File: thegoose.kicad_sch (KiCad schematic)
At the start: 45 parts, among them U1 DRV8848, U2 DRV8848, U3 DRV8848, U4 AP64500SP-13

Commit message: Connect everything except GPIO
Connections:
- net ESP_D12: no longer U1.9 (BIN1)
- net ESP_D13: no longer U1.10 (BIN2)
- net ESP_D14: no longer U1.15 (AIN2)
- net ESP_D15: no longer S6.1 (Pin_1)
- net ESP_D16: no longer S2.1 (Pin_1)
- net ESP_D17: no longer S3.1 (Pin_1)
- net ESP_D18: no longer S5.1 (Pin_1)
- net ESP_D19: no longer U3.16 (AIN1)
- net ESP_D21: no longer U3.15 (AIN2)
- net ESP_D22: no longer U3.9 (BIN1)
- net ESP_D23: no longer U3.10 (BIN2)
- net ESP_D25: no longer U2.9 (BIN1)
- net ESP_D26: no longer U2.10 (BIN2)
- net ESP_D27: no longer U1.16 (AIN1)
- net ESP_D32: no longer U2.16 (AIN1)
- net ESP_D33: no longer U2.15 (AIN2)
- net ESP_D4: no longer S1.1 (Pin_1)
- net ESP_D5: no longer S4.1 (Pin_1)
- net at U3.5 (BOUT2): now also M6.1 (OUT1); no longer M6.2 (OUT2)
- net at U3.7 (BOUT1): now also M6.2 (OUT2); no longer M6.1 (OUT1)
- net at M2.1 (OUT1): now also U1.5 (BOUT2); no longer U1.7 (BOUT1)
- net at M2.2 (OUT2): now also U1.7 (BOUT1); no longer U1.5 (BOUT2)
- net at M4.1 (OUT1): now also U2.5 (BOUT2); no longer U2.7 (BOUT1)
- net at M4.2 (OUT2): now also U2.7 (BOUT1); no longer U2.5 (BOUT2)

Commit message: Disconnect GPIO on schematic
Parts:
- removed C12, C5, C8: 100uF, Capacitor_SMD:C_1206_3216Metric_Pad1.33x1.80mm_HandSolder, symbol Device:C_Polarized

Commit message: First iteration of PCB
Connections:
- net ESP_D12: now also S2.1 (Pin_1)
- net ESP_D13: now also S1.1 (Pin_1)
- net ESP_D14: now also U3.15 (AIN2)
- net ESP_D15: now also U1.9 (BIN1)
- net ESP_D16: now also U1.15 (AIN2)
- net ESP_D17: now also U1.16 (AIN1)
- net ESP_D18: now also U2.10 (BIN2)
- net ESP_D19: now also U2.15 (AIN2)
- net ESP_D21: now also U2.16 (AIN1)
- net ESP_D22: now also U3.9 (BIN1)
- net ESP_D23: now also U3.10 (BIN2)
- net ESP_D25: now also S4.1 (Pin_1)
- net ESP_D26: now also S3.1 (Pin_1)
- net ESP_D27: now also U3.16 (AIN1)
- net ESP_D32: now also S6.1 (Pin_1)
- net ESP_D33: now also S5.1 (Pin_1)
- net ESP_D4: now also U1.10 (BIN2)
- net ESP_D5: now also U2.9 (BIN1)
- net at M3.1 (OUT1): now also U2.5 (BOUT2); no longer U2.2 (AOUT1)
- net at M3.2 (OUT2): now also U2.7 (BOUT1); no longer U2.4 (AOUT2)
- net at U3.2 (AOUT1): now also M6.1 (OUT1); no longer M5.1 (OUT1)
- net at U3.4 (AOUT2): now also M6.2 (OUT2); no longer M5.2 (OUT2)
- net at U3.5 (BOUT2): now also M5.1 (OUT1); no longer M6.1 (OUT1)
- net at U3.7 (BOUT1): now also M5.2 (OUT2); no longer M6.2 (OUT2)
- net at M2.1 (OUT1): now also U1.2 (AOUT1); no longer U1.5 (BOUT2)
- net at M2.2 (OUT2): now also U1.4 (AOUT2); no longer U1.7 (BOUT1)
- net at M4.1 (OUT1): now also U2.2 (AOUT1); no longer U2.5 (BOUT2)
- net at M4.2 (OUT2): now also U2.4 (AOUT2); no longer U2.7 (BOUT1)
- net at M1.1 (OUT1): now also U1.5 (BOUT2); no longer U1.2 (AOUT1)
- net at M1.2 (OUT2): now also U1.7 (BOUT1); no longer U1.4 (AOUT2)
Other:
- moved on the sheet: M1, M2, M3, M4, M5, M6

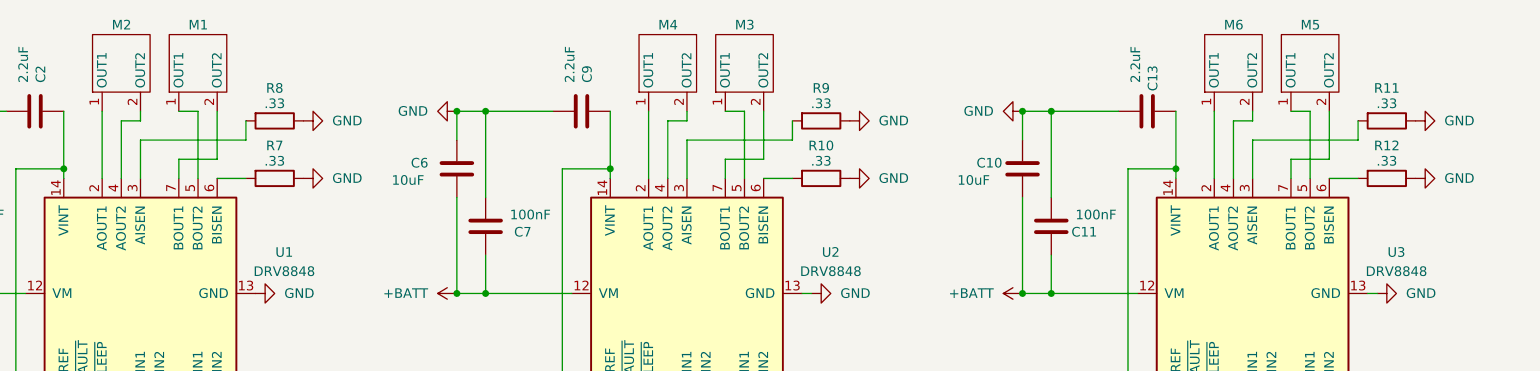
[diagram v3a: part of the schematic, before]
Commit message: Remove current shunt resistors
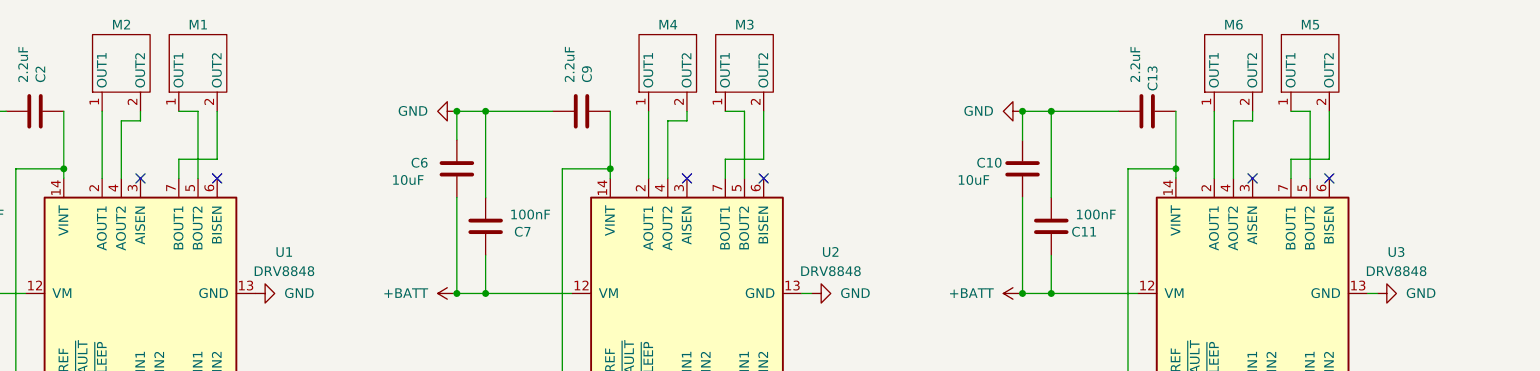
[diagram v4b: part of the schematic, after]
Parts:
- removed R10, R11, R12, R7, R8, R9: .33, Resistor_SMD:R_0805_2012Metric_Pad1.20x1.40mm_HandSolder, symbol Device:R
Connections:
- no-connect marks 10 -> 16

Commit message: Newify layout
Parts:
- BT1: value XT30_SOLDER_CABLE -> XT60; footprint hexy:XT30_SolderPads_1x02_P5.00mm -> hexy:AMASS_XT60PW-M_1x02_P7.20mm_Horizontal
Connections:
- net ESP_D15: now also U1.16 (AIN1); no longer U1.9 (BIN1)
- net ESP_D16: now also U1.9 (BIN1); no longer U1.15 (AIN2)
- net ESP_D17: now also U1.10 (BIN2); no longer U1.16 (AIN1)
- net ESP_D18: now also U2.15 (AIN2); no longer U2.10 (BIN2)
- net ESP_D19: now also U2.9 (BIN1); no longer U2.15 (AIN2)
- net ESP_D21: now also U2.10 (BIN2); no longer U2.16 (AIN1)
- net ESP_D22: now also U3.10 (BIN2); no longer U3.9 (BIN1)
- net ESP_D23: now also U3.9 (BIN1); no longer U3.10 (BIN2)
- net ESP_D4: now also U1.15 (AIN2); no longer U1.10 (BIN2)
- net ESP_D5: now also U2.16 (AIN1); no longer U2.9 (BIN1)
- net at M3.1 (OUT1): now also U2.2 (AOUT1); no longer U2.5 (BOUT2)
- net at M3.2 (OUT2): now also U2.4 (AOUT2); no longer U2.7 (BOUT1)
- net at U3.2 (AOUT1): now also M5.1 (OUT1); no longer M6.1 (OUT1)
- net at U3.4 (AOUT2): now also M5.2 (OUT2); no longer M6.2 (OUT2)
- net at U3.5 (BOUT2): now also M6.1 (OUT1); no longer M5.1 (OUT1)
- net at U3.7 (BOUT1): now also M6.2 (OUT2); no longer M5.2 (OUT2)
- net at M2.1 (OUT1): now also U1.5 (BOUT2); no longer U1.2 (AOUT1)
- net at M2.2 (OUT2): now also U1.7 (BOUT1); no longer U1.4 (AOUT2)
- net at M4.1 (OUT1): now also U2.5 (BOUT2); no longer U2.2 (AOUT1)
- net at M4.2 (OUT2): now also U2.7 (BOUT1); no longer U2.4 (AOUT2)
- net at M1.1 (OUT1): now also U1.2 (AOUT1); no longer U1.5 (BOUT2)
- net at M1.2 (OUT2): now also U1.4 (AOUT2); no longer U1.7 (BOUT1)
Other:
- moved on the sheet: C10, C11, C13, C2, C3, C4, C6, C7, C9, M1, M2, M3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

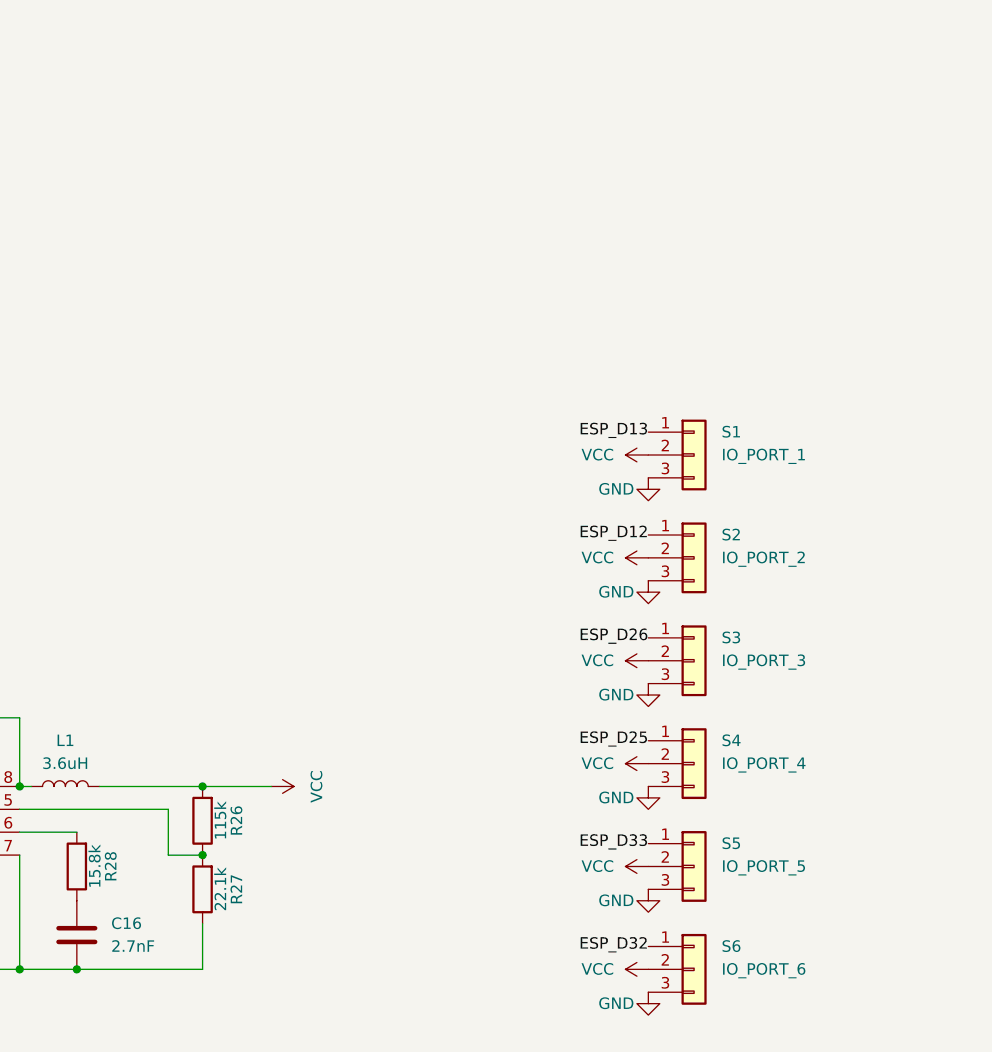
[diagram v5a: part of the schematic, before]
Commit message: Remove old separated gpio pins
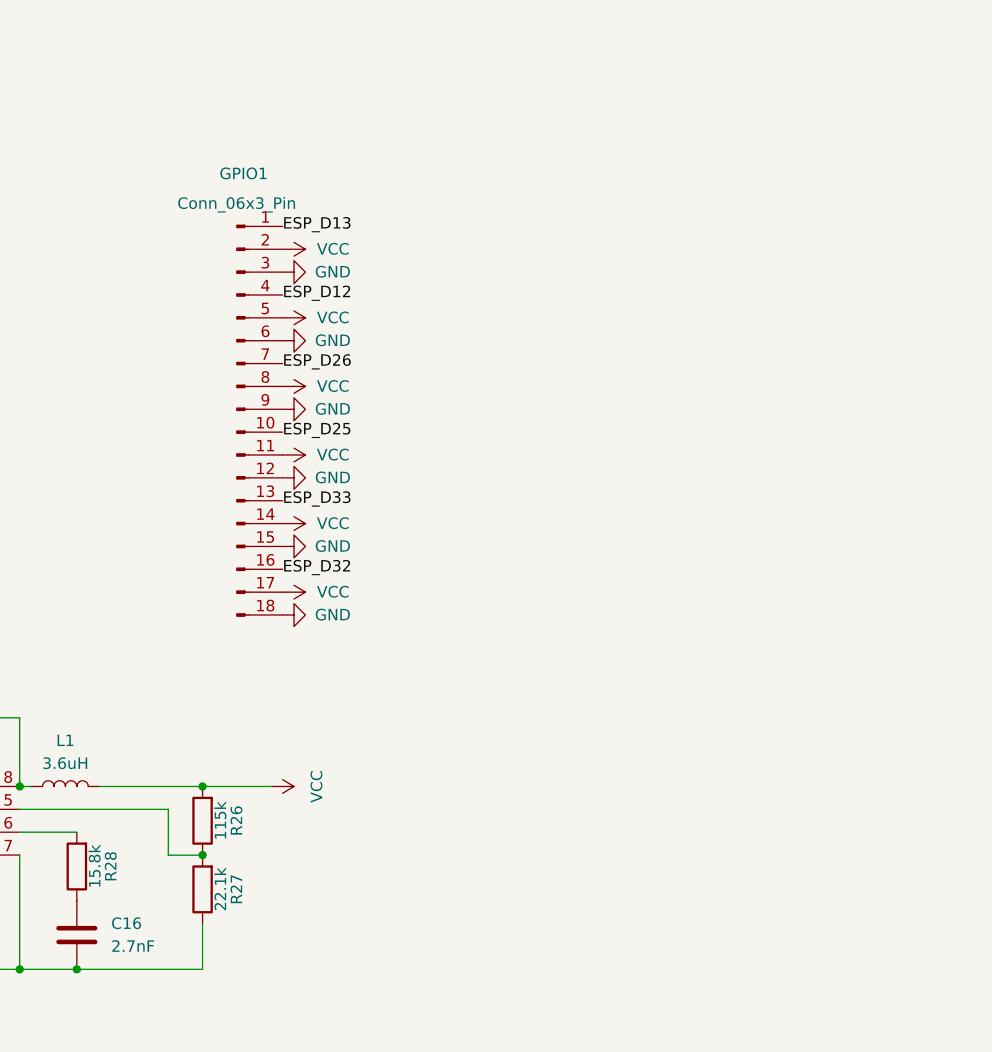
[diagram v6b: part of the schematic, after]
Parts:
- removed S1: IO_PORT_1, hexy:PinHeader_1x03_P2.54mm_Horizontal, symbol Connector_Generic:Conn_01x03
- removed S2: IO_PORT_2, hexy:PinHeader_1x03_P2.54mm_Horizontal, symbol Connector_Generic:Conn_01x03
- removed S3: IO_PORT_3, hexy:PinHeader_1x03_P2.54mm_Horizontal, symbol Connector_Generic:Conn_01x03
- removed S4: IO_PORT_4, hexy:PinHeader_1x03_P2.54mm_Horizontal, symbol Connector_Generic:Conn_01x03
- removed S5: IO_PORT_5, hexy:PinHeader_1x03_P2.54mm_Horizontal, symbol Connector_Generic:Conn_01x03
- removed S6: IO_PORT_6, hexy:PinHeader_1x03_P2.54mm_Horizontal, symbol Connector_Generic:Conn_01x03
- added GPIO1: Conn_06x3_Pin, symbol Connector:Conn_01x18_Pin
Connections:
- net ESP_D12: now also GPIO1.4 (Pin_4)
- net ESP_D13: now also GPIO1.1 (Pin_1)
- net ESP_D25: now also GPIO1.10 (Pin_10)
- net ESP_D26: now also GPIO1.7 (Pin_7)
- net ESP_D32: now also GPIO1.16 (Pin_16)
- net ESP_D33: now also GPIO1.13 (Pin_13)
- net GND: now also GPIO1.12 (Pin_12), GPIO1.15 (Pin_15), GPIO1.18 (Pin_18), GPIO1.3 (Pin_3), GPIO1.6 (Pin_6), GPIO1.9 (Pin_9)
- net VCC: now also GPIO1.11 (Pin_11), GPIO1.14 (Pin_14), GPIO1.17 (Pin_17), GPIO1.2 (Pin_2), GPIO1.5 (Pin_5), GPIO1.8 (Pin_8)

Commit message: Complete PCB
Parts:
- GPIO1: footprint (none) -> hexy:PinHeader_3x06_P2.54mm_Horizontal
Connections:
- net ESP_D12: now also U1.15 (AIN2); no longer GPIO1.4 (Pin_4)
- net ESP_D13: now also U1.16 (AIN1); no longer GPIO1.1 (Pin_1)
- net ESP_D14: now also GPIO1.16 (Pin_16); no longer U3.15 (AIN2)
- net ESP_D15: now also U1.9 (BIN1); no longer U1.16 (AIN1)
- net ESP_D16: now also U2.16 (AIN1); no longer U1.9 (BIN1)
- net ESP_D17: now also U2.15 (AIN2); no longer U1.10 (BIN2)
- net ESP_D18: now also U2.9 (BIN1); no longer U2.15 (AIN2)
- net ESP_D19: now also U3.16 (AIN1); no longer U2.9 (BIN1)
- net ESP_D21: now also U3.15 (AIN2); no longer U2.10 (BIN2)
- net ESP_D25: now also GPIO1.7 (Pin_7); no longer GPIO1.10 (Pin_10)
- net ESP_D26: now also GPIO1.10 (Pin_10); no longer GPIO1.7 (Pin_7)
- net ESP_D27: now also GPIO1.13 (Pin_13); no longer U3.16 (AIN1)
- net ESP_D32: now also GPIO1.1 (Pin_1); no longer GPIO1.16 (Pin_16)
- net ESP_D33: now also GPIO1.4 (Pin_4); no longer GPIO1.13 (Pin_13)
- net ESP_D4: now also U1.10 (BIN2); no longer U1.15 (AIN2)
- net ESP_D5: now also U2.10 (BIN2); no longer U2.16 (AIN1)
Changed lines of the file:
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@@
-		)
-	)
-	(label "ESP_D32"
-		(at 106.68 139.7 0)
-		(effects
-			(font
-				(size 1.27 1.27)
-			)
-			(justify left)
 		)
 	)
 	(label "ESP_D26"
+		(at 106.68 124.46 0)
+		(effects
+			(font
+				(size 1.27 1.27)
+			)
+			(justify left)
+		)
+	)
+	(label "ESP_D25"
 		(at 106.68 116.84 0)
 		(effects
@@
 		)
 	)
-	(label "ESP_D15"
-		(at 238.76 67.31 270)
-		(effects
-			(font
-				(size 1.27 1.27)
-			)
-			(justify right)
-		)
-	)
-	(label "ESP_D12"
-		(at 106.68 109.22 0)
-		(effects
-			(font
-				(size 1.27 1.27)
-			)
-			(justify left)
-		)
-	)
-	(label "ESP_D18"
-		(at 168.91 67.31 270)
-		(effects
-			(font
-				(size 1.27 1.27)
-			)
-			(justify right)
-		)
-	)
-	(label "ESP_D21"
-		(at 176.53 67.31 270)
+	(label "ESP_D4"
+		(at 248.92 67.31 270)
 		(effects
 			(font
@@
 		)
 	)
+	(label "ESP_D33"
+		(at 106.68 109.22 0)
+		(effects
+			(font
+				(size 1.27 1.27)
+			)
+			(justify left)
+		)
+	)
+	(label "ESP_D15"
+		(at 246.38 67.31 270)
+		(effects
+			(font
+				(size 1.27 1.27)
+			)
+			(justify right)
+		)
+	)
+	(label "ESP_D13"
+		(at 238.76 67.31 270)
+		(effects
+			(font
+				(size 1.27 1.27)
+			)
+			(justify right)
+		)
+	)
+	(label "ESP_D19"
+		(at 95.25 67.31 270)
+		(effects
+			(font
+				(size 1.27 1.27)
+			)
+			(justify right)
+		)
+	)
+	(label "ESP_D17"
+		(at 168.91 67.31 270)
+		(effects
+			(font
+				(size 1.27 1.27)
+			)
+			(justify right)
+		)
+	)
 	(label "ESP_D27"
-		(at 95.25 67.31 270)
-		(effects
-			(font
-				(size 1.27 1.27)
-			)
-			(justify right)
-		)
-	)
-	(label "ESP_D5"
+		(at 106.68 132.08 0)
+		(effects
+			(font
+				(size 1.27 1.27)
+			)
+			(justify left)
+		)
+	)
+	(label "ESP_D32"
+		(at 106.68 101.6 0)
+		(effects
+			(font
+				(size 1.27 1.27)
+			)
+			(justify left)
+		)
+	)
+	(label "ESP_D12"
+		(at 241.3 67.31 270)
+		(effects
+			(font
+				(size 1.27 1.27)
+			)
+			(justify right)
+		)
+	)
+	(label "ESP_D16"
 		(at 166.37 67.31 270)
 		(effects
@@
 		)
 	)
-	(label "ESP_D25"
-		(at 106.68 124.46 0)
-		(effects
-			(font
-				(size 1.27 1.27)
-			)
-			(justify left)
-		)
-	)
-	(label "ESP_D17"
-		(at 248.92 67.31 270)
-		(effects
-			(font
-				(size 1.27 1.27)
-			)
-			(justify right)
-		)
-	)
 	(label "ESP_D14"
-		(at 97.79 67.31 270)
-		(effects
-			(font
-				(size 1.27 1.27)
-			)
-			(justify right)
-		)
-	)
-	(label "ESP_D4"
-		(at 241.3 67.31 270)
-		(effects
-			(font
-				(size 1.27 1.27)
-			)
-			(justify right)
-		)
-	)
-	(label "ESP_D19"
-		(at 173.99 67.31 270)
-		(effects
-			(font
-				(size 1.27 1.27)
-			)
-			(justify right)
+		(at 106.68 139.7 0)
+		(effects
+			(font
+				(size 1.27 1.27)
+			)
+			(justify left)
 		)
 	)
@@
 		)
 	)
+	(label "ESP_D5"
+		(at 176.53 67.31 270)
+		(effects
+			(font
+				(size 1.27 1.27)
+			)
+			(justify right)
+		)
+	)
 	(label "ESP_D22"
 		(at 105.41 67.31 270)
@@
 		)
 	)
+	(label "ESP_D21"
+		(at 97.79 67.31 270)
+		(effects
+			(font
+				(size 1.27 1.27)
+			)
+			(justify right)
+		)
+	)
 	(label "ESP_D2"
 		(at 161.29 67.31 270)
@@
 		)
 	)
-	(label "ESP_D16"
-		(at 246.38 67.31 270)
-		(effects
-			(font
-				(size 1.27 1.27)
-			)
-			(justify right)
-		)
-	)
-	(label "ESP_D13"
-		(at 106.68 101.6 0)
-		(effects
-			(font
-				(size 1.27 1.27)
-			)
-			(justify left)
-		)
-	)
-	(label "ESP_D33"
-		(at 106.68 132.08 0)
-		(effects
-			(font
-				(size 1.27 1.27)
-			)
-			(justify left)
+	(label "ESP_D18"
+		(at 173.99 67.31 270)
+		(effects
+			(font
+				(size 1.27 1.27)
+			)
+			(justify right)
 		)
 	)
@@
 			)
 		)
-		(property "Footprint" ""
+		(property "Footprint" "hexy:PinHeader_3x06_P2.54mm_Horizontal"
 			(at 101.6 121.92 0)
 			(effects

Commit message: Add LCSC part numbers
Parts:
- BT1: LCSC Part # (none) -> C98732
- C1: LCSC Part # (none) -> C106837
- C10, C15, C3, C6: LCSC Part # (none) -> C272880
- C11, C14, C4, C7: LCSC Part # (none) -> C344180
- C13, C2, C9: LCSC Part # (none) -> C76638
- C16: LCSC Part # (none) -> C1847101
- ESP32: LCSC Part # (none) -> C82899
- GPIO1: LCSC Part # (none) -> C42431837
- L1: LCSC Part # (none) -> C167779
- M1, M2, M3, M4, M5, M6: LCSC Part # (none) -> C157931
- R25: LCSC Part # (none) -> C844827
- R26: LCSC Part # (none) -> C5200544
- R27: LCSC Part # (none) -> C856785
- R28: LCSC Part # (none) -> C170028
- U1, U2, U3: LCSC Part # (none) -> C2863921
- U4: LCSC Part # (none) -> C2070920
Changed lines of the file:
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@@
 		(on_board yes)
 		(dnp no)
+		(property "LCSC Part #" "C344180")
 		(property "Reference" "C7"
 			(at 145.796 43.942 0)
@@
 		(dnp no)
 		(fields_autoplaced yes)
+		(property "LCSC Part #" "C272880")
 		(property "Reference" "C15"
 			(at 44.45 171.4499 0)
@@
 		(on_board yes)
 		(dnp no)
+		(property "LCSC Part #" "C157931")
 		(property "Reference" "M3"
 			(at 162.56 16.51 90)
@@
 		(on_board yes)
 		(dnp no)
+		(property "LCSC Part #" "C42431837")
 		(property "Reference" "GPIO1"
 			(at 102.362 95.758 0)
@@
 		(dnp no)
 		(fields_autoplaced yes)
+		(property "LCSC Part #" "C167779")
 		(property "Reference" "L1"
 			(at 82.55 158.75 90)
@@
 		(on_board yes)
 		(dnp no)
+		(property "LCSC Part #" "C82899")
 		(property "Reference" "ESP32"
 			(at 47.498 103.632 0)
@@
 		(on_board yes)
 		(dnp no)
+		(property "LCSC Part #" "C344180")
 		(property "Reference" "C11"
 			(at 74.676 43.942 0)
@@
 		(on_board yes)
 		(dnp no)
+		(property "LCSC Part #" "C844827")
 		(property "Reference" "R25"
 			(at 55.88 177.8 90)
@@
 		(on_board yes)
 		(dnp no)
+		(property "LCSC Part #" "C76638")
 		(property "Reference" "C2"
 			(at 225.552 21.844 0)
@@
 		(on_board yes)
 		(dnp no)
+		(property "LCSC Part #" "C2070920")
 		(property "Reference" "U4"
 			(at 64.77 164.592 0)
@@
 		(on_board yes)
 		(dnp no)
+		(property "LCSC Part #" "C5200544")
 		(property "Reference" "R26"
 			(at 101.6 167.64 90)
@@
 		(dnp no)
 		(fields_autoplaced yes)
+		(property "LCSC Part #" "C2863921")
 		(property "Reference" "U3"
 			(at 114.3 46.6246 90)
@@
 		(on_board yes)
 		(dnp no)
+		(property "LCSC Part #" "C98732")
 		(property "Reference" "BT1"
 			(at 39.37 158.75 0)
@@
 		(on_board yes)
 		(dnp no)
+		(property "LCSC Part #" "C157931")
 		(property "Reference" "M2"
 			(at 245.11 16.51 90)
@@
 		(on_board yes)
 		(dnp no)
+		(property "LCSC Part #" "C272880")
 		(property "Reference" "C6"
 			(at 129.794 34.798 0)
@@
 		(on_board yes)
 		(dnp no)
+		(property "LCSC Part #" "C106837")
 		(property "Reference" "C1"
 			(at 16.764 98.806 0)
@@
 		(on_board yes)
 		(dnp no)
+		(property "LCSC Part #" "C272880")
 		(property "Reference" "C10"
 			(at 58.674 34.798 0)
@@
 		(on_board yes)
 		(dnp no)
+		(property "LCSC Part #" "C344180")
 		(property "Reference" "C4"
 			(at 218.186 43.942 0)
@@
 		(on_board yes)
 		(dnp no)
+		(property "LCSC Part #" "C157931")
 		(property "Reference" "M4"
 			(at 172.72 16.51 90)
@@
 		(on_board yes)
 		(dnp no)
+		(property "LCSC Part #" "C157931")
 		(property "Reference" "M5"
 			(at 91.44 16.51 90)
@@
 		(on_board yes)
 		(dnp no)
+		(property "LCSC Part #" "C157931")
 		(property "Reference" "M1"
 			(at 234.95 16.51 90)
@@
 		(on_board yes)
 		(dnp no)
+		(property "LCSC Part #" "C157931")
 		(property "Reference" "M6"
 			(at 101.6 16.51 90)
@@
 		(on_board yes)
 		(dnp no)
+		(property "LCSC Part #" "C76638")
 		(property "Reference" "C9"
 			(at 153.162 21.844 0)
@@
 		(dnp no)
 		(fields_autoplaced yes)
+		(property "LCSC Part #" "C1847101")
 		(property "Reference" "C16"
 			(at 87.63 179.0699 0)
@@
 		(on_board yes)
 		(dnp no)
+		(property "LCSC Part #" "C76638")
 		(property "Reference" "C13"
 			(at 82.042 21.844 0)
@@
 		(on_board yes)
 		(dnp no)
+		(property "LCSC Part #" "C856785")
 		(property "Reference" "R27"
 			(at 101.6 175.26 90)
@@
 		(on_board yes)
 		(dnp no)
+		(property "LCSC Part #" "C272880")
 		(property "Reference" "C3"
 			(at 202.184 34.798 0)
@@
 		(on_board yes)
 		(dnp no)
+		(property "LCSC Part #" "C170028")
 		(property "Reference" "R28"
 			(at 87.63 172.72 90)
@@
 		(on_board yes)
 		(dnp no)
+		(property "LCSC Part #" "C344180")
 		(property "Reference" "C14"
 			(at 65.532 150.114 0)
@@
 		(dnp no)
 		(fields_autoplaced yes)
+		(property "LCSC Part #" "C2863921")
 		(property "Reference" "U2"
 			(at 185.42 46.6246 90)
@@
 		(dnp no)
 		(fields_autoplaced yes)
+		(property "LCSC Part #" "C2863921")
 		(property "Reference" "U1"
 			(at 257.81 46.6246 90)
